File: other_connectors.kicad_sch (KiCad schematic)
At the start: 3 parts, among them J1 Conn_01x06, J4 Conn_01x02

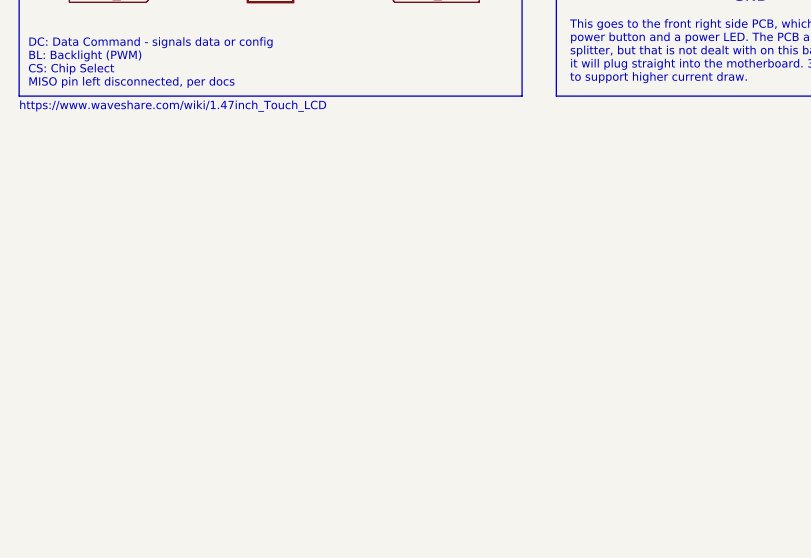
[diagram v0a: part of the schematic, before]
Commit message: Made preliminary TUSB1064 schematic
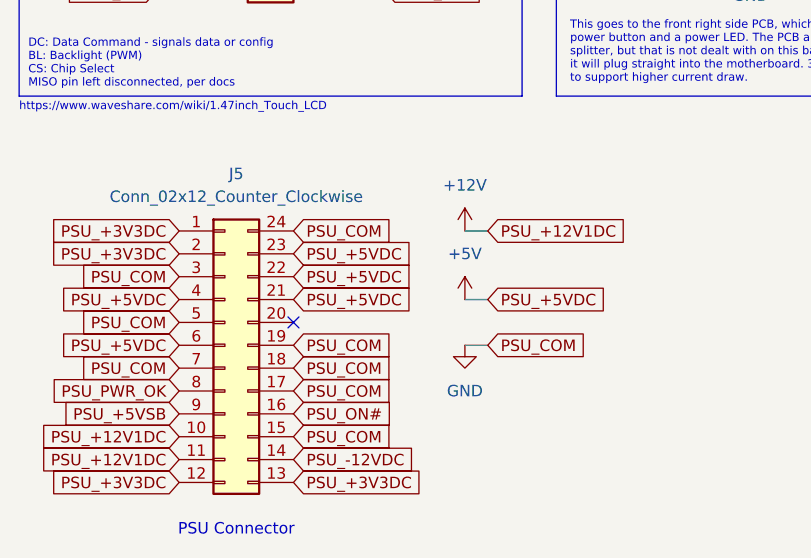
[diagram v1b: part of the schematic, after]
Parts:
- added J5: Conn_02x12_Counter_Clockwise, Connector_Molex:Molex_Mini-Fit_Jr_5566-24A_2x12_P4.20mm_Vertical, symbol Connector_Generic:Conn_02x12_Counter_Clockwise
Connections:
- net +5V: now also J5.21 (Pin_21), J5.22 (Pin_22), J5.23 (Pin_23), J5.4 (Pin_4), J5.6 (Pin_6)
- net GND: now also J5.15 (Pin_15), J5.17 (Pin_17), J5.18 (Pin_18), J5.19 (Pin_19), J5.24 (Pin_24), J5.3 (Pin_3), J5.5 (Pin_5), J5.7 (Pin_7)
- new net +12V: J5.10 (Pin_10), J5.11 (Pin_11)
- new net PSU_+3V3DC: J5.1 (Pin_1), J5.12 (Pin_12), J5.13 (Pin_13), J5.2 (Pin_2)
- new net PSU_+5VSB: J5.9 (Pin_9)
- new net PSU_-12VDC: J5.14 (Pin_14)
- new net PSU_ON#: J5.16 (Pin_16)
- new net PSU_PWR_OK: J5.8 (Pin_8)
- no-connect marks 0 -> 1
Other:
- note added: "PSU Connector"

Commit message: Preliminary revision of USB hub and temperature monitor
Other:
- moved on the sheet: J1, J4, J5, TOUCH_DISP_CONN0

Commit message: Preliminary design of power monitor for PSU rails and USB-C VBUS
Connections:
- net +5V: no longer J5.21 (Pin_21), J5.22 (Pin_22), J5.23 (Pin_23), J5.4 (Pin_4), J5.6 (Pin_6)
- net +12V renamed PSU_+12V1DC
- new net PSU_+5VDC: J5.21 (Pin_21), J5.22 (Pin_22), J5.23 (Pin_23), J5.4 (Pin_4), J5.6 (Pin_6)

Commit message: Preliminary design of power monitor for PS176, TC358743, LicheeRV nano, and touch display
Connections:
- net +3V3 renamed +3V3_DISP
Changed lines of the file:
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@@
 		(in_pos_files yes)
 		(dnp no)
-		(fields_autoplaced yes)
 		(property "Reference" "#PWR0140"
 			(at 39.37 29.21 0)
@@
 			)
 		)
-		(property "Value" "+3V3"
-			(at 31.75 29.2099 90)
+		(property "Value" "+3V3_DISP"
+			(at 27.178 29.21 90)
 			(show_name no)
 			(do_not_autoplace no)
@@
 					(size 1.27 1.27)
 				)
-				(justify left)
 			)
 		)

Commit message: Preliminary design of power monitor for USB2244i, 2xRTL9210b + SSD, front panel hub, and 4x chassis fans
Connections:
- net +5V renamed +5V_PANEL
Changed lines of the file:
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@@
 	(wire
 		(pts
-			(xy 97.79 30.48) (xy 101.6 30.48)
+			(xy 95.25 30.48) (xy 101.6 30.48)
 		)
 		(stroke
@@
 	(symbol
 		(lib_id "power:+1V1")
-		(at 97.79 30.48 0)
+		(at 95.25 30.48 0)
 		(unit 1)
 		(body_style 1)
@@
 		(dnp no)
 		(property "Reference" "#PWR0124"
-			(at 97.79 34.29 0)
-			(hide yes)
-			(show_name no)
-			(do_not_autoplace no)
-			(effects
-				(font
-					(size 1.27 1.27)
-				)
-			)
-		)
-		(property "Value" "+5V"
-			(at 96.012 26.67 0)
+			(at 95.25 34.29 0)
+			(hide yes)
+			(show_name no)
+			(do_not_autoplace no)
+			(effects
+				(font
+					(size 1.27 1.27)
+				)
+			)
+		)
+		(property "Value" "+5V_PANEL"
+			(at 89.408 26.416 0)
 			(show_name no)
 			(do_not_autoplace no)
@@
 		)
 		(property "Footprint" ""
-			(at 97.79 30.48 0)
+			(at 95.25 30.48 0)
 			(hide yes)
 			(show_name no)
@@
 		)
 		(property "Datasheet" ""
-			(at 97.79 30.48 0)
+			(at 95.25 30.48 0)
 			(hide yes)
 			(show_name no)
@@
 		)
 		(property "Description" "Power symbol creates a global label with name \"+1V1\""
-			(at 97.79 30.48 0)
-			(hide yes)
-			(show_name no)
+			(at 95.25 30.48 0)
+			(hide yes)
+			(show_name no)
